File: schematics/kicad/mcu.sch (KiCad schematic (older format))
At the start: 1 part, among them U4 STELLARIS_LAUNCHPAD

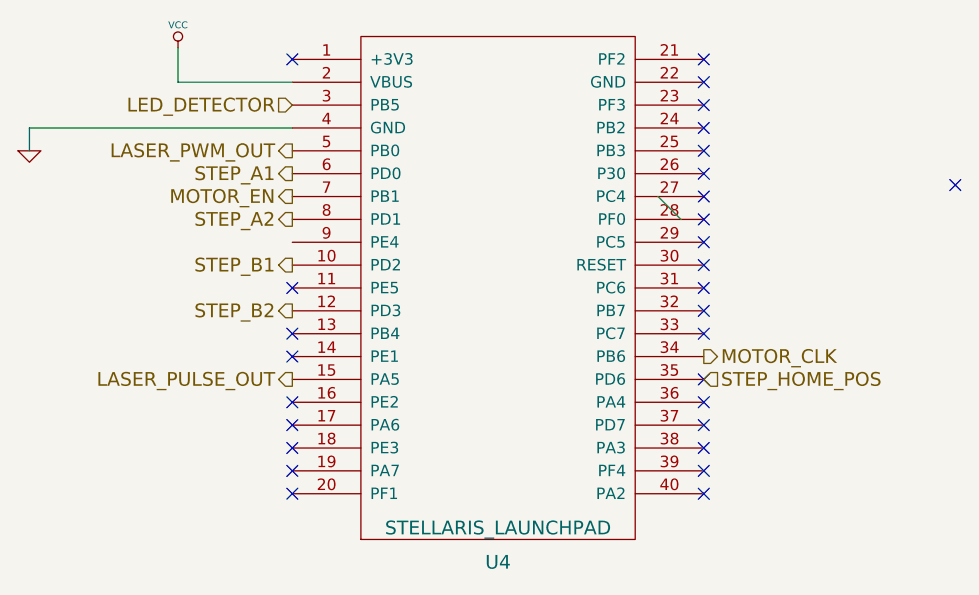
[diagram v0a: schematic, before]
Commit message: Updated schematics to match the code (and, reality)
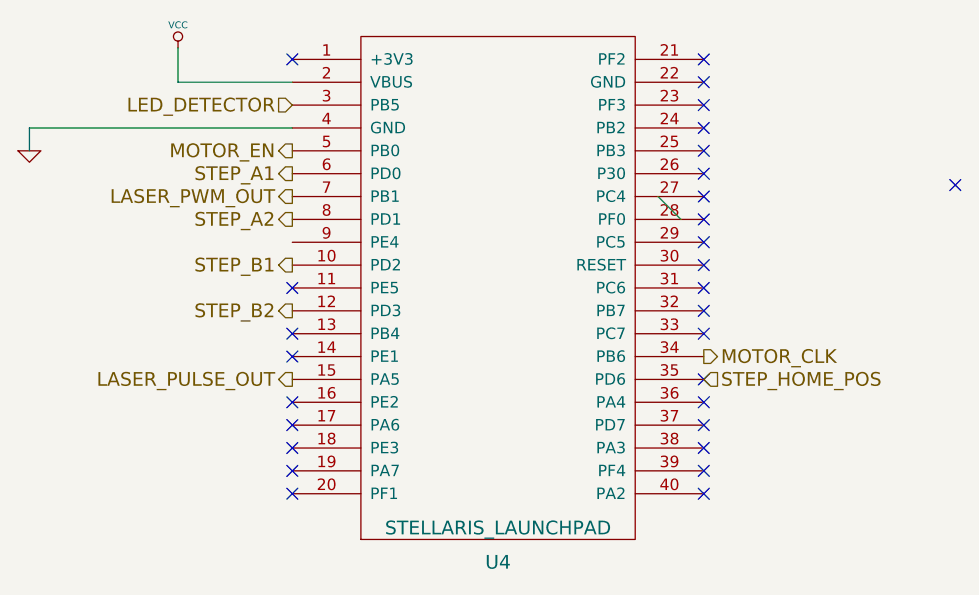
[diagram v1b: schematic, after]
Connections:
- net LASER_PWM_OUT: now also U4.7 (PB1); no longer U4.5 (PB0)
- net MOTOR_EN: now also U4.5 (PB0); no longer U4.7 (PB1)
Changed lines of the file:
@@
-EESchema Schematic File Version 2  date ceturtdiena, 2013. gada  9. maijs, plkst. 01 un 37
+EESchema Schematic File Version 2  date svētdiena, 2013. gada 19. maijs, plkst. 23 un 38
 LIBS:power
 LIBS:device
@@
 Sheet 2 4
 Title "Lasershow"
-Date "8 may 2013"
+Date "19 may 2013"
 Rev ""
 Comp "Hackerspace"
@@
 	1    0    0    -1
 $EndComp
-Text HLabel 3750 2950 0    60   Output ~ 0
+Text HLabel 3750 2750 0    60   Output ~ 0
 MOTOR_EN
 Text HLabel 5550 3650 2    60   Output ~ 0
@@
 	2600 2650 2600 2750
 $Comp
-L GND #PWR05
+L GND #PWR5
 U 1 1 517FDBED
 P 2600 2750
-F 0 "#PWR05" H 2600 2750 30  0001 C CNN
+F 0 "#PWR5" H 2600 2750 30  0001 C CNN
 F 1 "GND" H 2600 2680 30  0001 C CNN
 F 2 "" H 2600 2750 60  0000 C CNN
@@
 Text HLabel 3750 3750 0    60   Output ~ 0
 LASER_PULSE_OUT
-Text HLabel 3750 2750 0    60   Output ~ 0
+Text HLabel 3750 2950 0    60   Output ~ 0
 LASER_PWM_OUT
 Text HLabel 3750 2850 0    60   Output ~ 0
@@
 NoConn ~ 5550 2350
 $Comp
-L VCC #PWR06
+L VCC #PWR6
 U 1 1 51802907
 P 3250 2300
-F 0 "#PWR06" H 3250 2400 30  0001 C CNN
+F 0 "#PWR6" H 3250 2400 30  0001 C CNN
 F 1 "VCC" H 3250 2400 30  0000 C CNN
 F 2 "" H 3250 2300 60  0000 C CNN
